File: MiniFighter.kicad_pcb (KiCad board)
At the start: 2 copper layers, 213.4 x 119.4 mm, 50 parts, among them K1 SW_SPST, K2 SW_SPST, K3 SW_SPST, K4 SW_SPST, M3.1 MountingHole, M3.2 MountingHole, M3.3 MountingHole, M3.4 MountingHole, M3.5 MountingHole, M3.6 MountingHole, P1 SW_SPST, P2 SW_SPST, P3 SW_SPST, P4 SW_SPST, U1 Pico

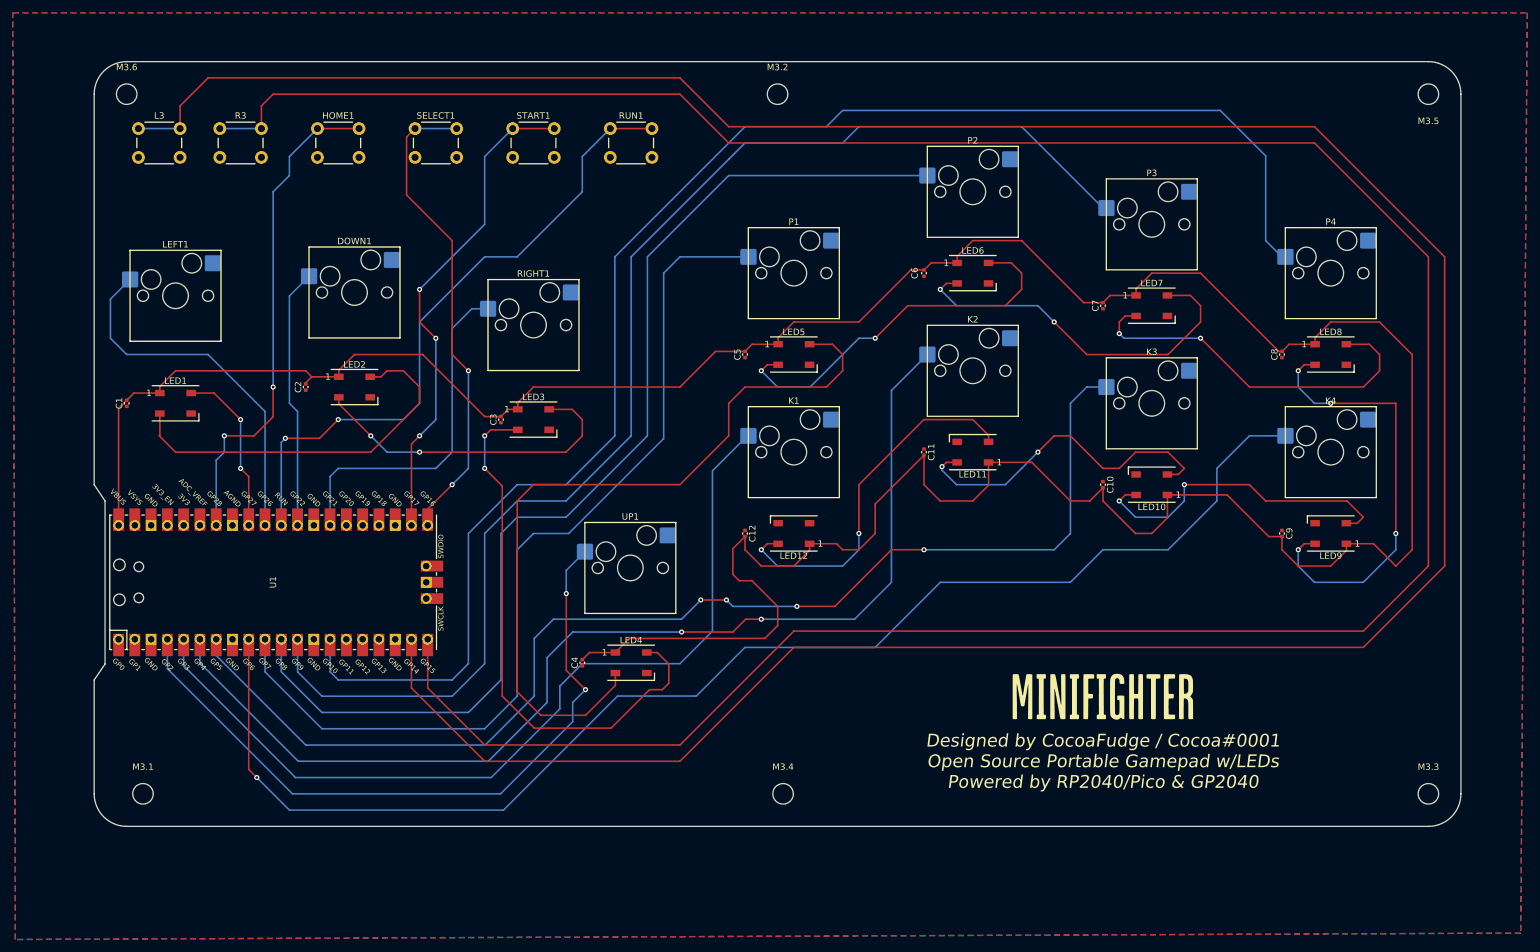
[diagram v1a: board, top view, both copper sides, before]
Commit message: Add files via upload
Updated the PCB design, made it smaller in dimensions. Button positions and LED placement have NOT CHANGED.
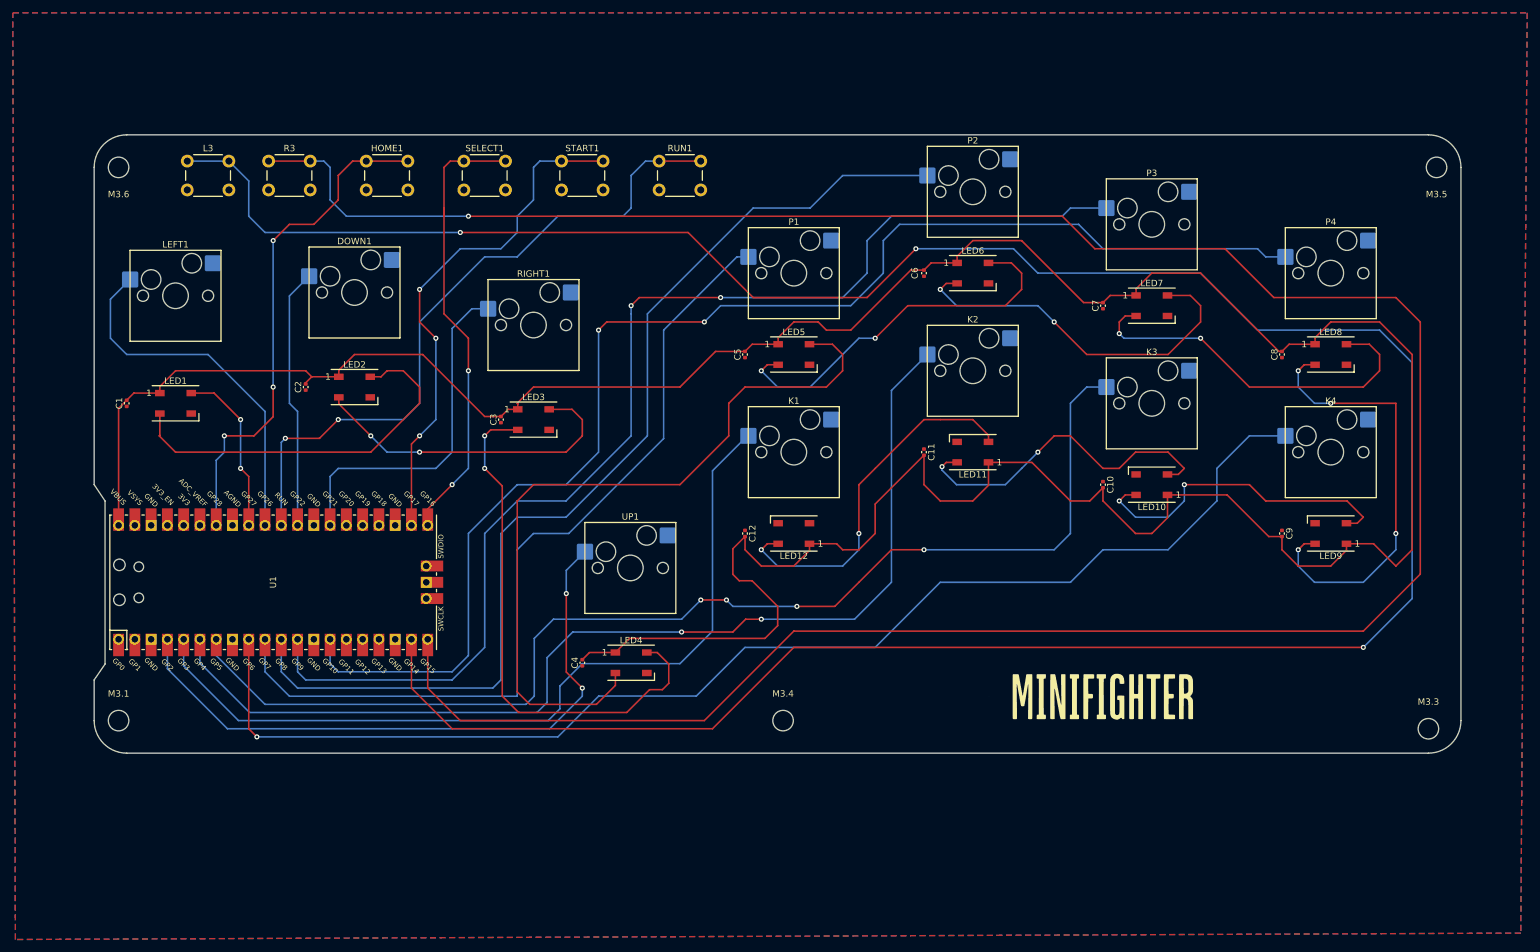
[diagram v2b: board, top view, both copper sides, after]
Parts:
- removed M3.2: MountingHole, MountingHole:MountingHole_3.2mm_M3
- moved M3.1 12.0 mm to (372.1, 290.8)
- moved M3.5 11.5 mm to (577.9, 204.5)
- moved M3.6 11.5 mm to (372.1, 204.5), turned to 180 degrees
- moved M3.4 11.4 mm to (475.8, 290.8)
- moved M3.3 10.2 mm to (576.6, 292.1)
- moved HOME1 9.16 mm to (410.8, 203.5)
- moved L3 9.16 mm to (382.8, 203.5)
- moved RUN1 9.16 mm to (456.5, 203.5)
- moved SELECT1 9.16 mm to (426.0, 203.5)
- moved START1 9.16 mm to (441.2, 203.5)
- moved R3 9.16 mm to (395.5, 203.5)
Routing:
- net GP14: track 455.4 -> 425.5 mm, vias 0 -> 3
- net GP10: track 237.0 -> 209.8 mm, vias 0 -> 2
- net GP15: track 430.8 -> 406.7 mm, vias 0 -> 1
- net GP 9: track 203.3 -> 187.7 mm, vias 0 -> 2
- net GP 6: track 211.9 -> 198.8 mm
- net GP 2: track 110.4 -> 100.2 mm
- net GP 7: track 143.3 -> 133.8 mm
- net GP 8: track 173.1 -> 164.7 mm
- net GP 3: track 138.4 -> 131.0 mm
- net GP 4: track 171.6 -> 165.2 mm
- net RUN: track 101.8 -> 107.0 mm
- net GP 5: track 188.4 -> 183.2 mm
- net GP16: track 75.6 -> 71.4 mm
- net GP17: track 77.1 -> 80.9 mm
- net Net-(LED3-Pad2): track 85.5 -> 83.4 mm
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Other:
- board size 213.4 x 119.4 mm -> 213.4 x 96.5 mm
- board text removed: "Designed by CocoaFudge / Cocoa#0001 Open Source Portable Gamepad w/LEDs Powered by RP2040/Pico & GP2040"

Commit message: Smaller Dimensions. LAYOUT NOT CHANGED.
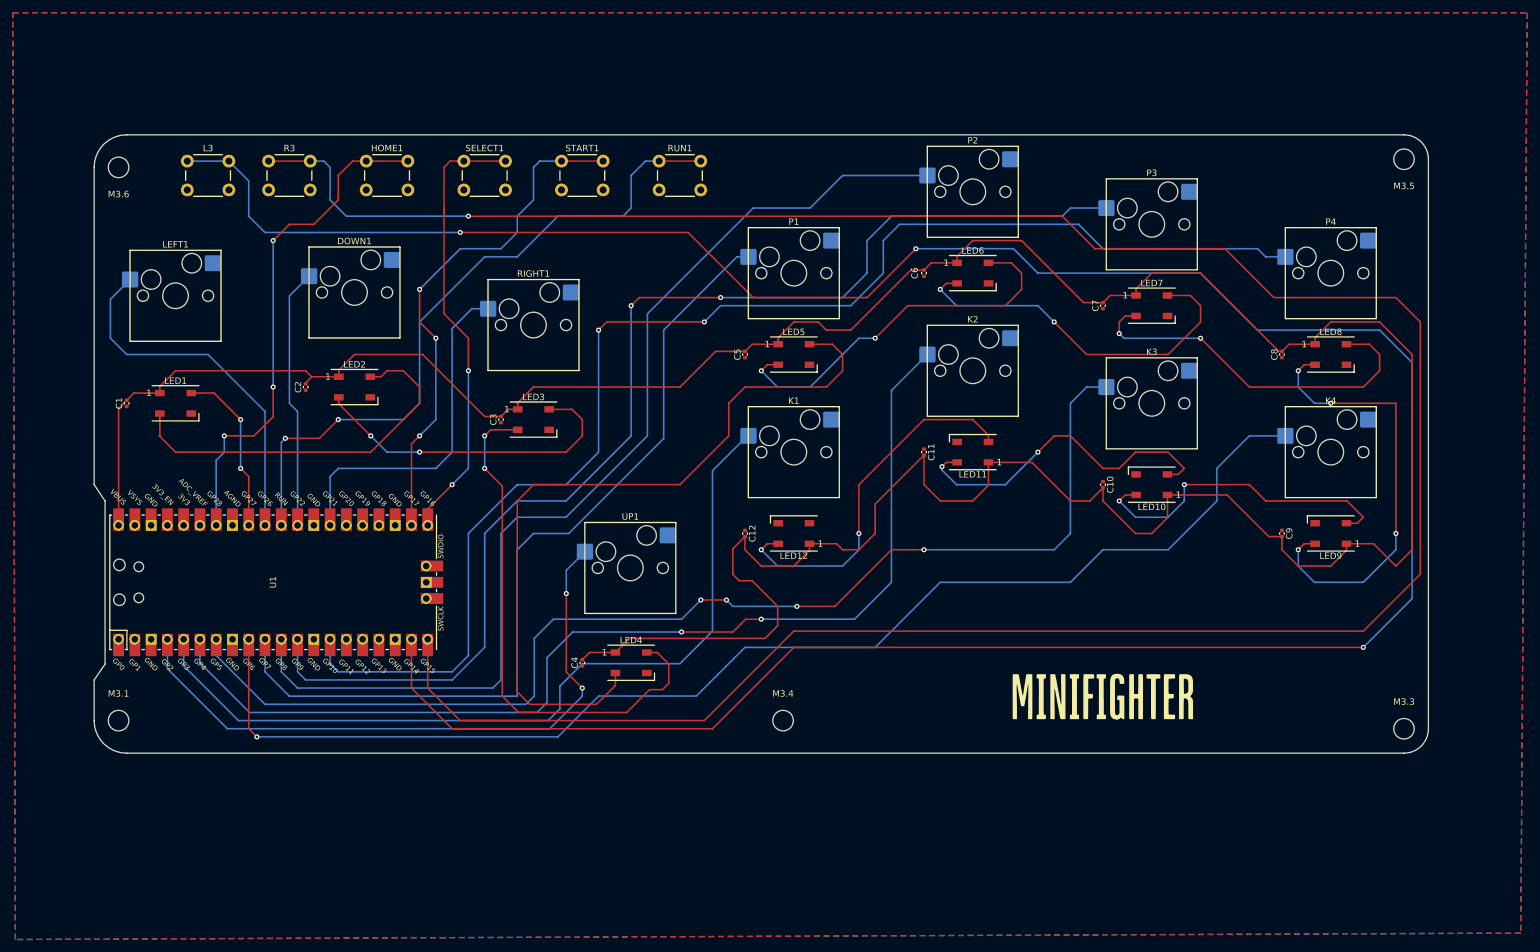
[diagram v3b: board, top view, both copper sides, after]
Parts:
- moved M3.5 5.24 mm to (572.8, 203.2)
- moved M3.3 3.81 mm to (572.8, 292.1)
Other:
- board size 213.4 x 96.5 mm -> 208.3 x 96.5 mm
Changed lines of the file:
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@@
   )
   (footprint "MountingHole:MountingHole_3.2mm_M3" (layer "F.Cu")
-    (at 576.58 292.1)
+    (at 572.77 292.1)
     (descr "Mounting Hole 3.2mm, no annular, M3")
     (tags "mounting hole 3.2mm no annular m3")
@@
   )
   (footprint "MountingHole:MountingHole_3.2mm_M3" (layer "F.Cu")
-    (at 577.85 204.47 180)
+    (at 572.77 203.2 180)
     (descr "Mounting Hole 3.2mm, no annular, M3")
     (tags "mounting hole 3.2mm no annular m3")
@@
   )
   (gr_line (start 370 282) (end 368.3 284.48) (layer "Edge.Cuts") (width 0.1))
-  (gr_arc (start 581.66 290.83) (mid 580.172102 294.422102) (end 576.58 295.91) (layer "Edge.Cuts") (width 0.1))
   (gr_arc (start 368.3 204.47) (mid 369.787898 200.877898) (end 373.38 199.39) (layer "Edge.Cuts") (width 0.1))
-  (gr_line (start 581.66 290.83) (end 581.66 204.47) (layer "Edge.Cuts") (width 0.1))
   (gr_line (start 370 282) (end 370 256.54) (layer "Edge.Cuts") (width 0.1))
-  (gr_line (start 373.38 295.91) (end 576.58 295.91) (layer "Edge.Cuts") (width 0.1))
+  (gr_arc (start 576.58 292.1) (mid 575.464077 294.794077) (end 572.77 295.91) (layer "Edge.Cuts") (width 0.1))
+  (gr_line (start 373.38 295.91) (end 572.77 295.91) (layer "Edge.Cuts") (width 0.1))
   (gr_line (start 370 256.54) (end 368.3 254) (layer "Edge.Cuts") (width 0.1))
-  (gr_arc (start 576.58 199.39) (mid 580.172102 200.877898) (end 581.66 204.47) (layer "Edge.Cuts") (width 0.1))
+  (gr_line (start 576.58 292.1) (end 576.58 203.2) (layer "Edge.Cuts") (width 0.1))
+  (gr_arc (start 572.77 199.39) (mid 575.464077 200.505923) (end 576.58 203.2) (layer "Edge.Cuts") (width 0.1))
   (gr_line (start 368.3 284.48) (end 368.3 290.83) (layer "Edge.Cuts") (width 0.1))
   (gr_line (start 368.3 204.47) (end 368.3 254) (layer "Edge.Cuts") (width 0.1))
   (gr_arc (start 373.38 295.91) (mid 369.787898 294.422102) (end 368.3 290.83) (layer "Edge.Cuts") (width 0.1))
-  (gr_line (start 576.58 199.39) (end 373.38 199.39) (layer "Edge.Cuts") (width 0.1))
+  (gr_line (start 572.77 199.39) (end 373.38 199.39) (layer "Edge.Cuts") (width 0.1))
   (segment (start 372.11 242.08307) (end 373.37307 240.82) (width 0.25) (layer "F.Cu") (net 2))
   (segment (start 551.66 262.1) (end 545.16 255.6) (width 0.25) (layer "F.Cu") (net 2))
